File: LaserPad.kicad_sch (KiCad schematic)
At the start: 20 parts, among them J1 USB_C_Receptacle_USB2.0_16P, SW1 RST, SW2 RST, U1 STM32F072CBTx, U3 PRTR5V0U2X, U4 USBLC6-2SC6, U5 XC6206PxxxMR-Regulator_Linear

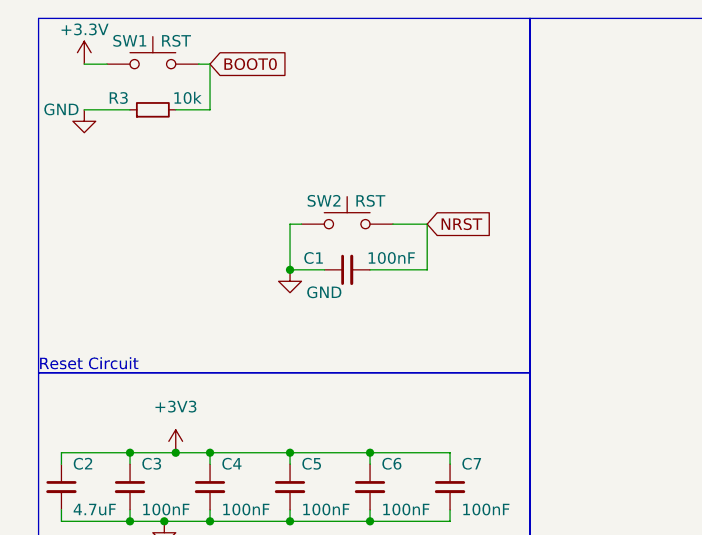
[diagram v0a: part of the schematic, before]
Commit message: Changed reset circuit into something that will hopefully take up less space on pcb
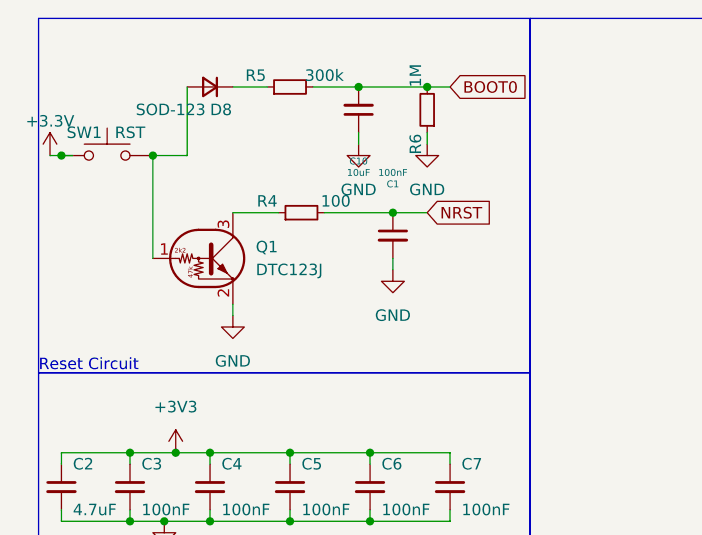
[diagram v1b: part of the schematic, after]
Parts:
- removed R3: 10k, Resistor_SMD:R_0402_1005Metric, symbol Device:R_Small
- removed SW2: RST, Button_Switch_SMD:SW_SPST_SKQG_WithoutStem, symbol Switch:SW_Push
- added C10: 10uF, Capacitor_SMD:C_0402_1005Metric, symbol Device:C_Small
- added D8: SOD-123, Diode_SMD:D_SOD-123, symbol Device:D_Small
- added Q1: DTC123J, symbol Transistor_BJT:DTC123J
- added R4: 100, Resistor_SMD:R_0402_1005Metric, symbol Device:R_Small
- added R5: 300k, Resistor_SMD:R_0402_1005Metric, symbol Device:R_Small
- added R6: 1M, Resistor_SMD:R_0402_1005Metric, symbol Device:R_Small
- C1: LCSC C307331 -> C52923
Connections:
- net BOOT0: now also C10.2, R5.2, R6.2; no longer SW1.2
- net GND: now also C1.2, C10.1, Q1.2 (E), R6.1; no longer C1.1
- net NRST: now also C1.1, R4.2; no longer C1.2
- new net: D8.1 (K), R5.1
- new net: D8.2 (A), Q1.1 (B), SW1.2
- new net: Q1.3 (C), R4.1
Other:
- moved on the sheet: SW1

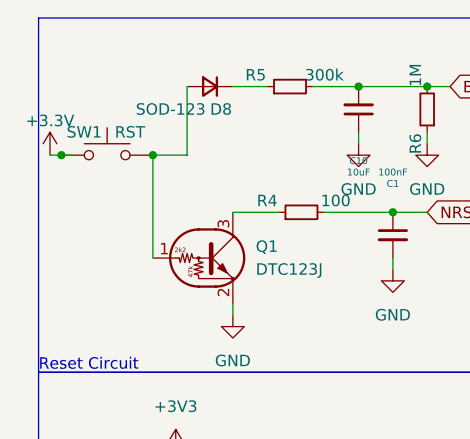
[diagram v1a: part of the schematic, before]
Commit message: Changed around a couple of objects for new reset circuit
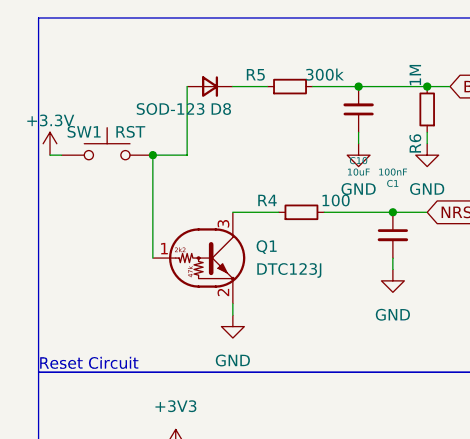
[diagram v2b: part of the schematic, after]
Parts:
- Q1: footprint (none) -> Package_TO_SOT_SMD:SOT-23
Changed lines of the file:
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@@
   (junction (at 22.86 60.96) (diameter 0) (color 0 0 0 0)
-  )
-  (junction (at 15.24 27.94) (diameter 0) (color 0 0 0 0)
   )
   (junction (at 55.88 20.32) (diameter 0) (color 0 0 0 0)
@@
     (stroke (width 0) (type default))
   )
-  (wire (pts (xy 13.97 27.94) (xy 15.24 27.94))
-    (stroke (width 0) (type default))
-  )
   (wire (pts (xy 58.42 67.31) (xy 58.42 68.58))
-    (stroke (width 0) (type default))
-  )
-  (wire (pts (xy 15.24 27.94) (xy 16.51 27.94))
     (stroke (width 0) (type default))
   )
@@
   )
   (wire (pts (xy 251.46 38.1) (xy 254 38.1))
+    (stroke (width 0) (type default))
+  )
+  (wire (pts (xy 13.97 27.94) (xy 15.24 27.94))
     (stroke (width 0) (type default))
   )
@@
       (effects (font (size 1.27 1.27)) (justify left))
     )
-    (property "Footprint" "" (at 31.75 39.37 0)
+    (property "Footprint" "Package_TO_SOT_SMD:SOT-23" (at 31.75 39.37 0)
       (effects (font (size 1.27 1.27)) (justify left) hide)
     )

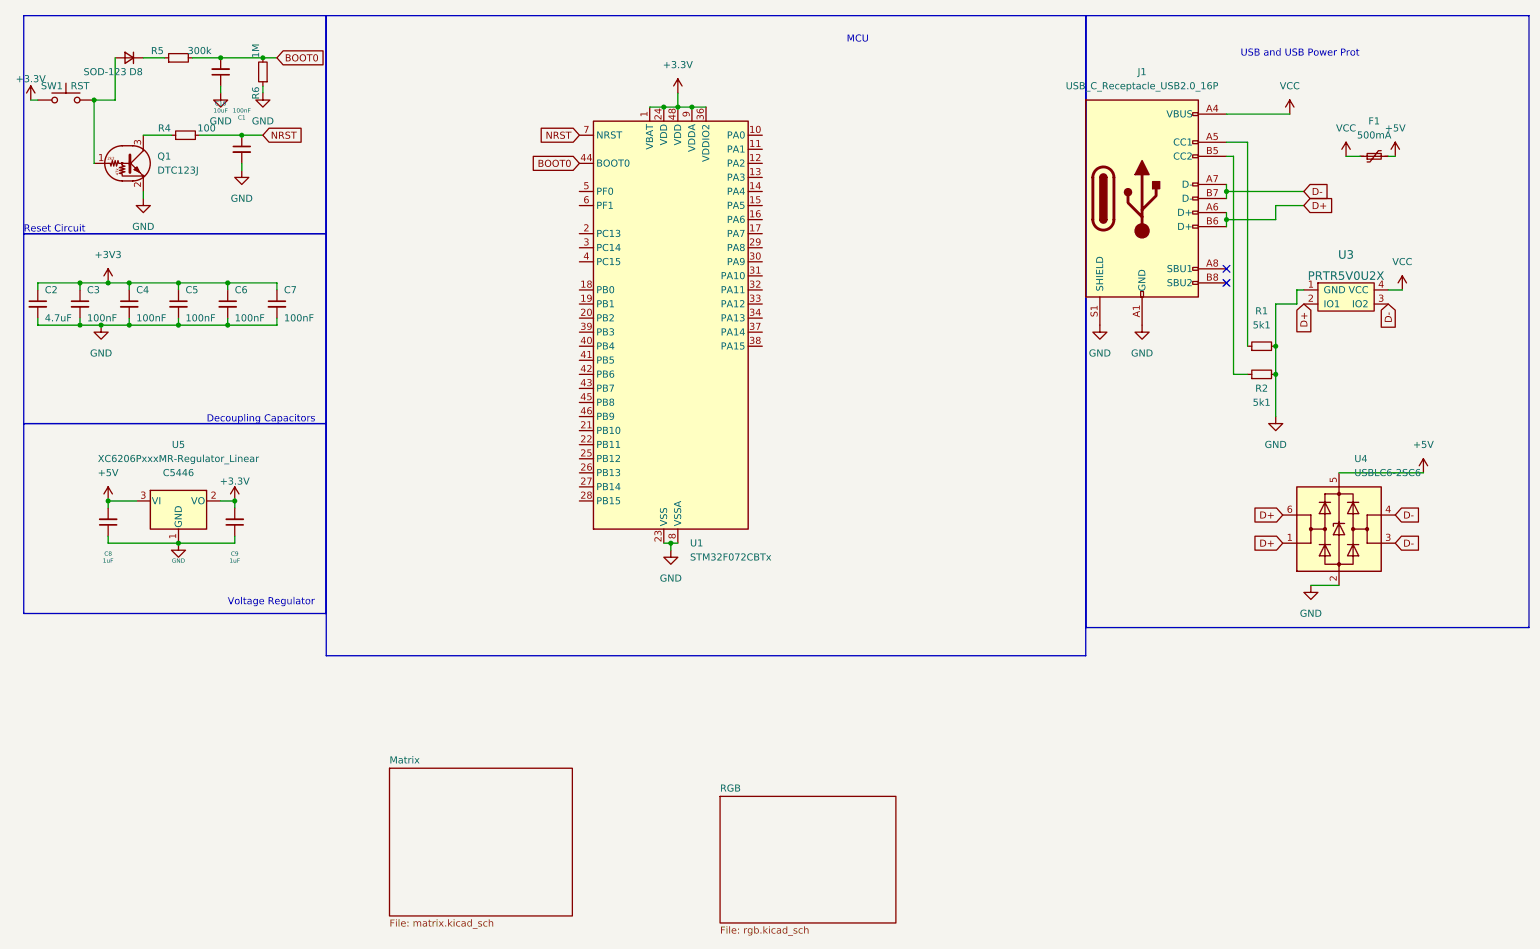
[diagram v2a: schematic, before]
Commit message: Changed reset circuit yet again :/
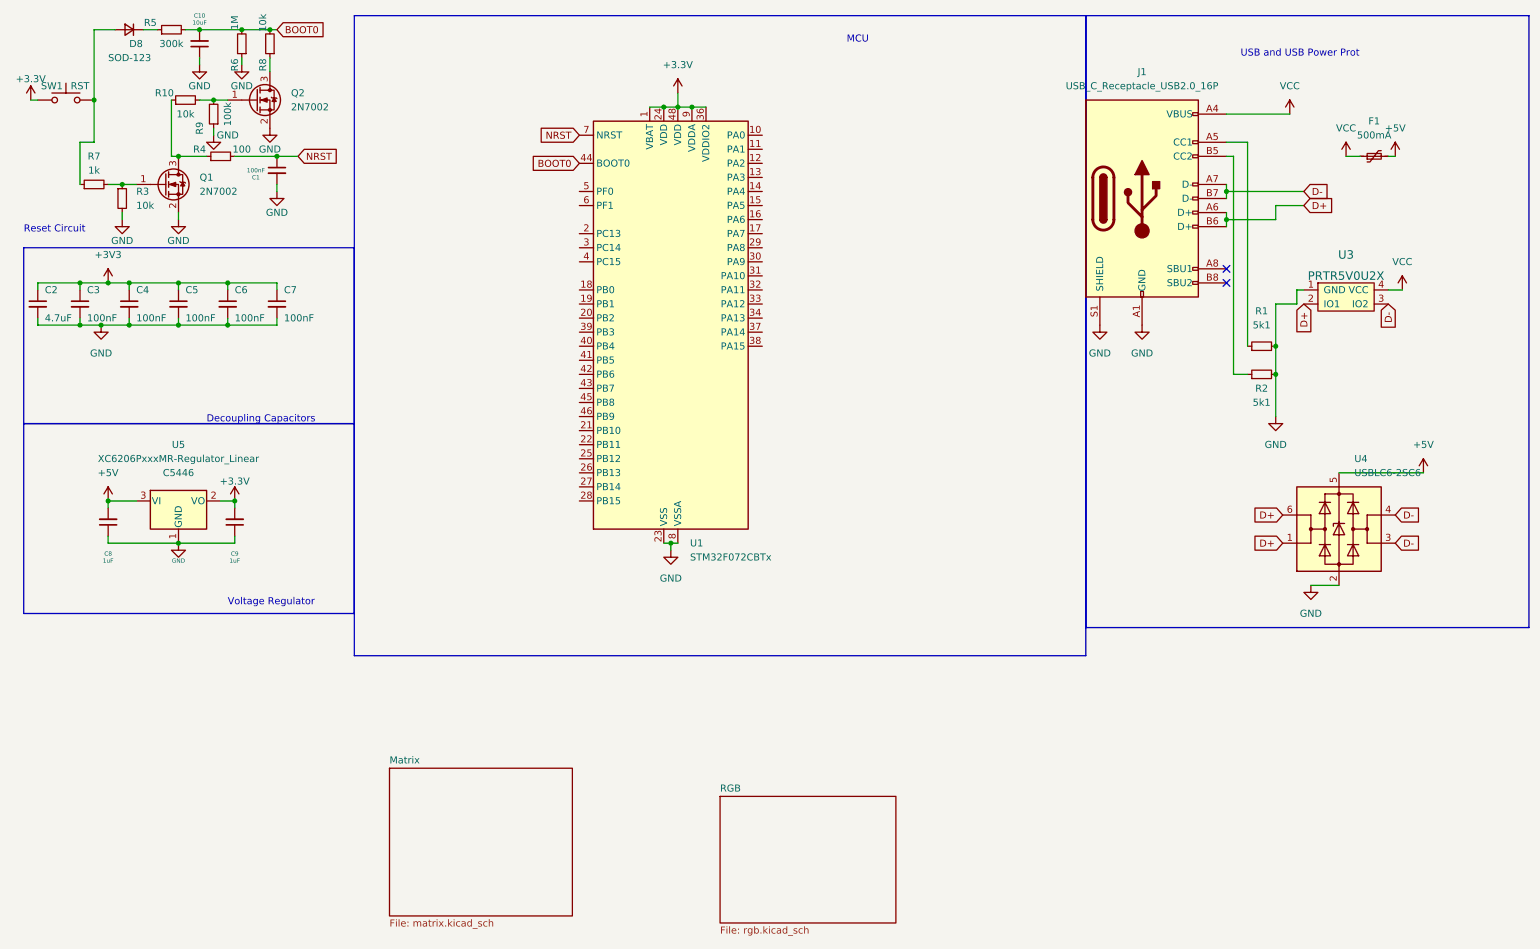
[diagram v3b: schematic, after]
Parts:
- removed Q1: DTC123J, Package_TO_SOT_SMD:SOT-23, symbol Transistor_BJT:DTC123J
- added Q1, Q2: 2N7002, Package_TO_SOT_SMD:SOT-23, symbol Transistor_FET:2N7002
- added R10, R3, R8: 10k, Resistor_SMD:R_0402_1005Metric, symbol Device:R_Small
- added R7: 1k, Resistor_SMD:R_0402_1005Metric, symbol Device:R_Small
- added R9: 100k, Resistor_SMD:R_0402_1005Metric, symbol Device:R_Small
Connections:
- net BOOT0: now also R8.2
- net GND: now also Q1.2 (S), Q2.2 (S), R3.2, R9.1
- net at D8.2 (A), SW1.2: now also R7.1
- net at R4.1: now also Q1.3 (D), R10.1
- new net: Q2.3 (D), R8.1
- new net: Q1.1 (G), R3.1, R7.2
- new net: Q2.1 (G), R10.2, R9.2
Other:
- moved on the sheet: C1, C10, D8, R4, R5, R6
